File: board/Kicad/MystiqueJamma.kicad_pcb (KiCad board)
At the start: 2 copper layers, 140.4 x 114.8 mm, 143 parts, among them IC1 7805, IC10 TDA2030V, IC11 LA4425V, IC2 74HC4021D, IC3 74LS245DW, IC4 74HC4021D, IC5 CY7C1049CV33, IC6 TDA1543T, IC7 74LS245DW, IC8 TLS1233, IC9 74HC4021D, J1 Conn_01x04, K1 JAMMA-EDGE-MYSTIQUE, X2 1503_09, X4 HF15H

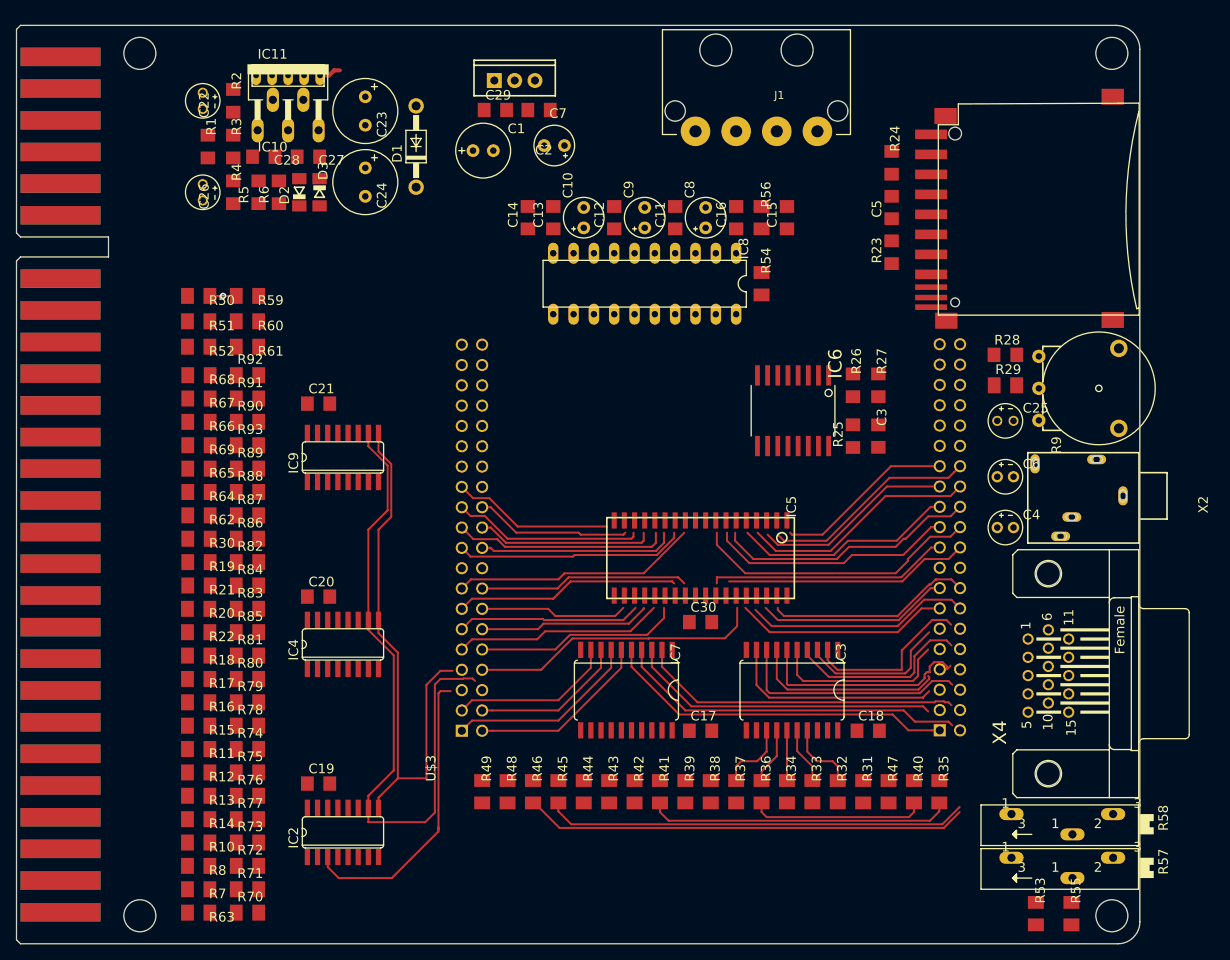
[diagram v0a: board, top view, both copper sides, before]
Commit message: Added edge cut for JTAG header
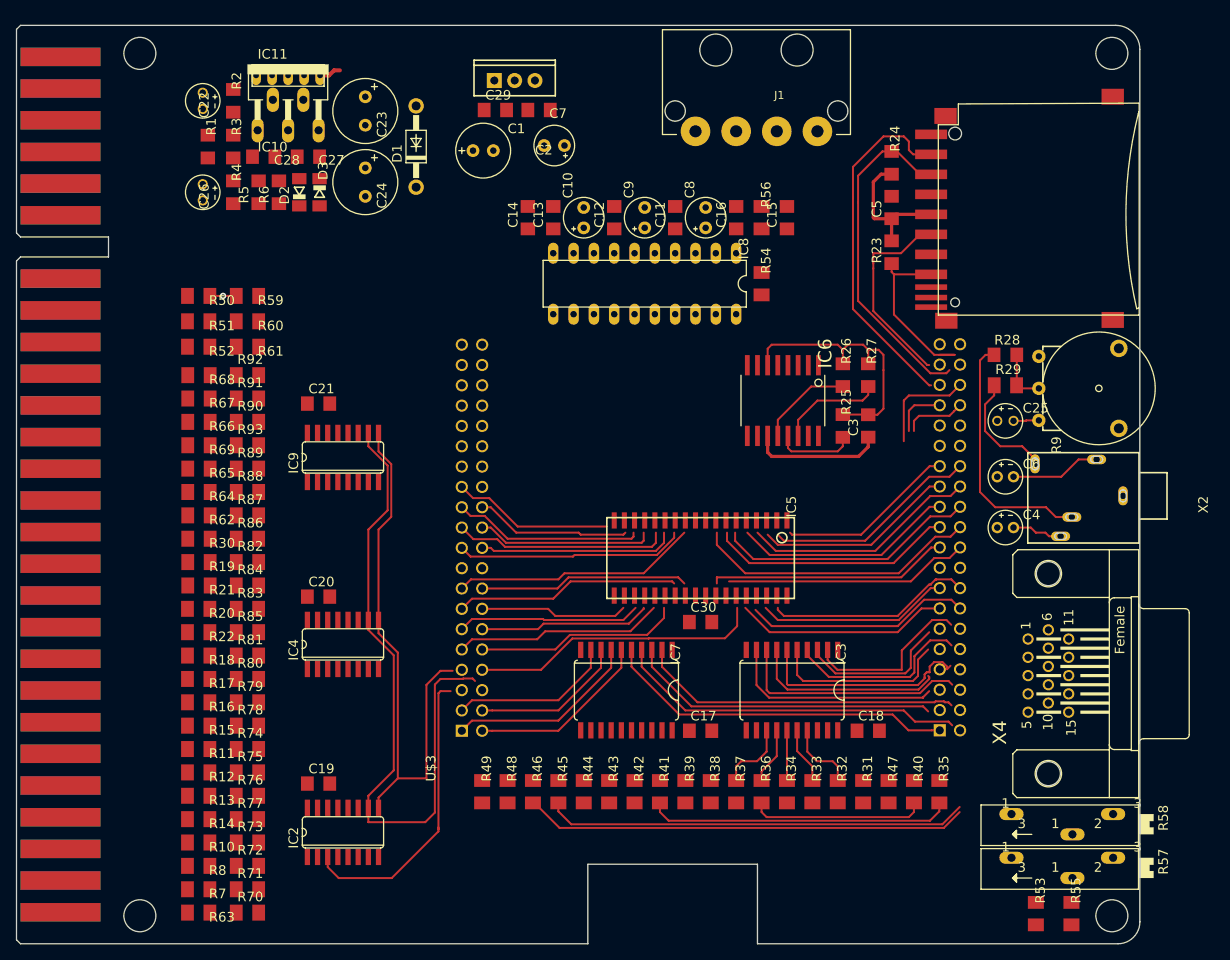
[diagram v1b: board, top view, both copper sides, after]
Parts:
- moved C3 1.80 mm to (173.4, 81.9), turned to 90 degrees
- moved R27 1.80 mm to (173.4, 75.6)
- moved IC6 1.80 mm to (162.7, 78.7)
- moved R25 1.80 mm to (170.2, 81.9), turned to 270 degrees
- moved R26 1.80 mm to (170.2, 75.6)
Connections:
- J1 pad 1: Net-(J1-Pad1) -> +12V
- J1 pad 2: Net-(J1-Pad2) -> GND
- J1 pad 3: Net-(J1-Pad3) -> GND
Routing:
- net /SD_CS: track 0.00 -> 44.4 mm
- net /SD_DATAIN: track 0.00 -> 42.6 mm
- net GND: track 0.00 -> 33.4 mm
- net Net-(R28-Pad1): track 0.00 -> 31.3 mm
- net /SD_SCLK: track 0.00 -> 25.2 mm
- net /SD_DATAOUT: track 0.00 -> 22.7 mm
- net +3V3: track 0.00 -> 17.4 mm
- net +5V: track 0.00 -> 16.6 mm
- net Net-(R29-Pad1): track 0.00 -> 14.5 mm
- net /R_A: track 0.00 -> 13.1 mm
- net Net-(U$3-PadI0_105): track 0.00 -> 12.9 mm
- net /L_A: track 0.00 -> 11.9 mm
- net /L_AUDIO: track 0.00 -> 11.3 mm
- net /DAC_VREF: track 0.00 -> 9.93 mm
- net Net-(U$3-PadI0_110): track 0.00 -> 7.85 mm
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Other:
- outline, holes or cut-outs redrawn

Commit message: Edge connector pins associated with shift registers
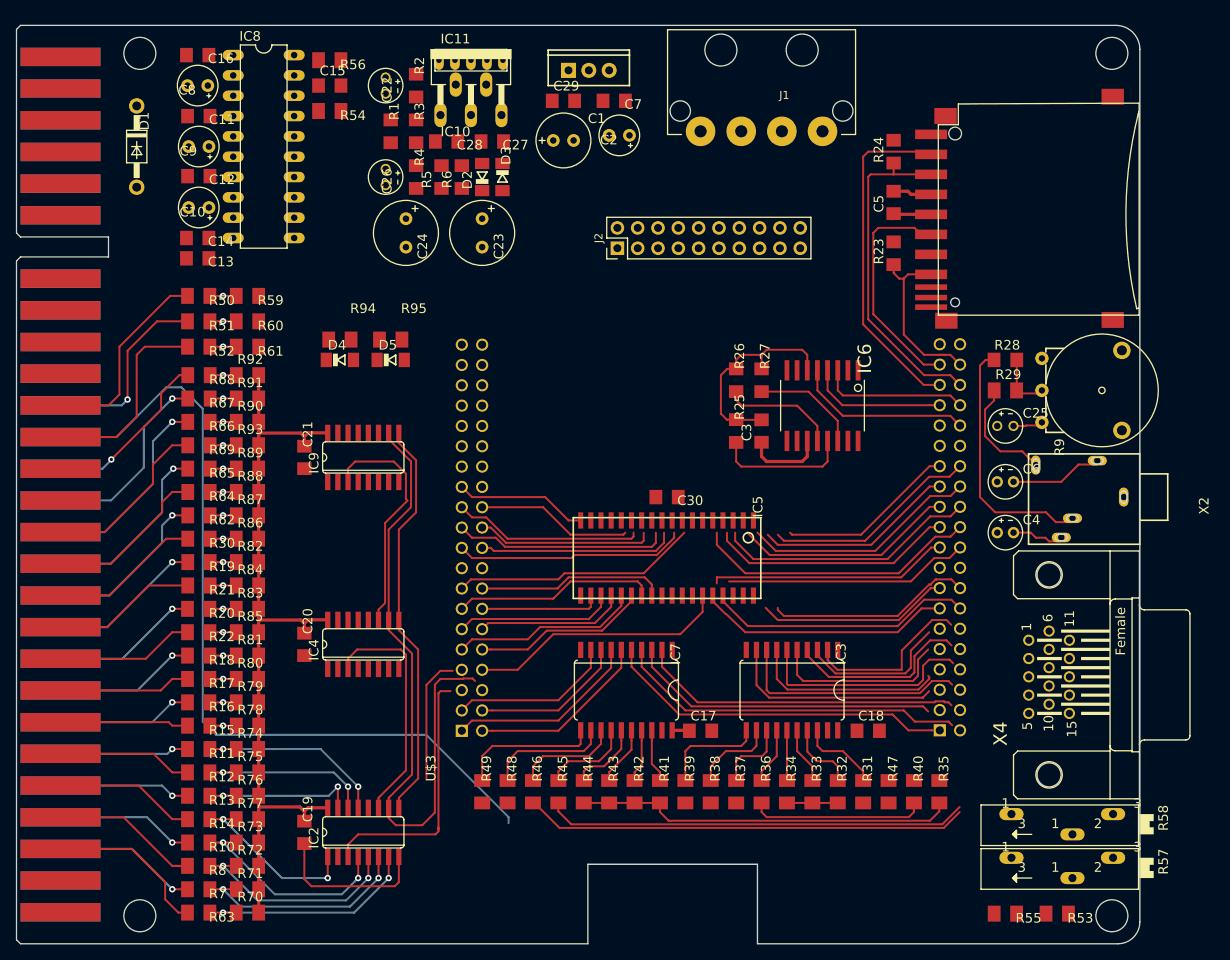
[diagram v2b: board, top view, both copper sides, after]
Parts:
- added D4: 4148, MystiqueJamma:SOD80C, F.Cu at (107.3, 73.7)
- added D5: 4148, MystiqueJamma:SOD80C, F.Cu at (113.7, 73.7)
- added J2: Conn_02x10_Odd_Even, Connector_PinHeader_2.54mm:PinHeader_2x10_P2.54mm_Vertical, F.Cu at (142.0, 59.7)
- added R94: 330, MystiqueJamma:M1206, F.Cu at (107.3, 71.1)
- added R95: 330, MystiqueJamma:M1206, F.Cu at (113.7, 71.1)
- moved C16 70.3 mm to (89.5, 35.6), turned to 180 degrees
- moved C8 65.6 mm to (89.5, 39.4), turned to 180 degrees
- moved C11 60.9 mm to (89.7, 43.2), turned to 180 degrees
- moved C15 59.5 mm to (106.0, 39.4), turned to 0 degrees
- moved R54 58.1 mm to (106.0, 42.5), turned to 180 degrees
- moved R56 57.5 mm to (106.0, 36.2), turned to 180 degrees
- moved C9 56.4 mm to (89.7, 47.0), turned to 180 degrees
- moved C12 52.2 mm to (89.7, 50.7), turned to 180 degrees
- moved IC8 50.6 mm to (97.8, 47.0), turned to 270 degrees
- moved C10 48.1 mm to (89.7, 54.6), turned to 180 degrees
- moved C13 44.7 mm to (89.5, 61.0), turned to 180 degrees
- moved C14 41.4 mm to (89.5, 58.4), turned to 180 degrees
- moved D1 34.9 mm to (81.9, 47.0), turned to 270 degrees
- moved C27 23.1 mm to (126.4, 46.4)
- moved R6 22.9 mm to (122.6, 50.8)
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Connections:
- net Net-(K1-Pad8) renamed /COIN_CT1
- net Net-(K1-PadJ) renamed /COIN_CT2
- IC9 pad 11: GND -> Net-(D4-PadA)
- K1 pad #A: Net-(K1-Pad#A) -> /P2B2
- K1 pad #B: Net-(K1-Pad#B) -> /P2B3
- K1 pad #C: Net-(K1-Pad#C) -> /P2B4
- K1 pad #D: Net-(K1-Pad#D) -> /P2B5
- K1 pad M: Net-(K1-PadM) -> GND
- K1 pad R: Net-(K1-PadR) -> /SERVICE_SW
- K1 pad S: Net-(K1-PadS) -> /TILT
- K1 pad T: Net-(K1-PadT) -> /COINSW2
- K1 pad U: Net-(K1-PadU) -> /P2START
- K1 pad V: Net-(K1-PadV) -> /P2UP
- K1 pad W: Net-(K1-PadW) -> /P2DW
- K1 pad X: Net-(K1-PadX) -> /P2LH
- K1 pad Y: Net-(K1-PadY) -> /P2RH
- K1 pad Z: Net-(K1-PadZ) -> /P2B1
- R10 pad 2: /N$62 -> /P2B4
- R11 pad 2: /N$64 -> /P2B2
- R12 pad 2: /N$63 -> /P1B2
- R13 pad 2: /N$65 -> /P2B3
- R14 pad 2: /N$66 -> /P1B3
- R15 pad 2: /N$68 -> /P1B1
- R16 pad 2: /N$67 -> /P2B1
- R17 pad 2: /N$69 -> /P1RH
- R18 pad 2: /N$70 -> /P2RH
- R19 pad 2: /N$72 -> /P2DW
- R20 pad 2: /N$73 -> /P2LH
- R21 pad 2: /N$74 -> /P1DW
- R22 pad 2: /N$76 -> /P1LH
- R30 pad 2: /N$75 -> /P1UP
- R62 pad 2: /N$77 -> /P2UP
- R63 pad 2: /N$47 -> /P1B5
- R64 pad 2: /N$78 -> /P1START
- R65 pad 2: /N$80 -> /P2START
- R66 pad 2: /N$79 -> /COINSW2
- R67 pad 2: /N$81 -> /TILT
- R68 pad 2: /N$82 -> /SERVICE_SW
- R69 pad 2: /VGA_DETECT -> /COINSW1
- R7 pad 2: /N$46 -> /P2B5
- R8 pad 2: /N$61 -> /P1B4
- U$3 pad I0_1: Net-(U$3-PadI0_1) -> /G2
- U$3 pad I0_10: Net-(U$3-PadI0_10) -> /B2
- U$3 pad I0_101: Net-(U$3-PadI0_101) -> /SD_SCLK
- U$3 pad I0_103: Net-(U$3-PadI0_103) -> /SD_DATAOUT
- U$3 pad I0_104: Net-(U$3-PadI0_104) -> /SD_CS
- U$3 pad I0_105: Net-(U$3-PadI0_105) -> /SD_DATAIN
- U$3 pad I0_106: Net-(U$3-PadI0_106) -> /IS2_WS
- U$3 pad I0_110: Net-(U$3-PadI0_110) -> /I2S_BCK
- U$3 pad I0_112: Net-(U$3-PadI0_112) -> /I2S_DATA
- U$3 pad I0_115: Net-(U$3-PadI0_115) -> /SRAM_A0
- U$3 pad I0_119: Net-(U$3-PadI0_119) -> /SRAM_A1
- U$3 pad I0_120: Net-(U$3-PadI0_120) -> /SRAM_A2
- U$3 pad I0_121: Net-(U$3-PadI0_121) -> /SRAM_A3
- U$3 pad I0_124: Net-(U$3-PadI0_124) -> /SRAM_A4
- U$3 pad I0_125: Net-(U$3-PadI0_125) -> /SRAM_CE
- U$3 pad I0_126: Net-(U$3-PadI0_126) -> /SRAM_IO0
- U$3 pad I0_127: Net-(U$3-PadI0_127) -> /SRAM_IO1
- U$3 pad I0_128: Net-(U$3-PadI0_128) -> /SRAM_IO6
- U$3 pad I0_129: Net-(U$3-PadI0_129) -> /SRAM_IO7
- U$3 pad I0_132: Net-(U$3-PadI0_132) -> /SRAM_A18
- U$3 pad I0_133: Net-(U$3-PadI0_133) -> /SRAM_A17
- U$3 pad I0_135: Net-(U$3-PadI0_135) -> /SRAM_A16
- U$3 pad I0_136: Net-(U$3-PadI0_136) -> /SRAM_A15
- U$3 pad I0_137: Net-(U$3-PadI0_137) -> /R0
- U$3 pad I0_138: Net-(U$3-PadI0_138) -> /R1
- U$3 pad I0_141: Net-(U$3-PadI0_141) -> /R2
- U$3 pad I0_142: Net-(U$3-PadI0_142) -> /R3
- U$3 pad I0_143: Net-(U$3-PadI0_143) -> /G0
- U$3 pad I0_144: Net-(U$3-PadI0_144) -> /G1
- U$3 pad I0_2: Net-(U$3-PadI0_2) -> /G3
- U$3 pad I0_3: Net-(U$3-PadI0_3) -> /B0
- U$3 pad I0_33: Net-(U$3-PadI0_33) -> /CNTR_DAT
- U$3 pad I0_34: Net-(U$3-PadI0_34) -> /CNTR_CLK
- U$3 pad I0_38: Net-(U$3-PadI0_38) -> /CNTR_LATCH
- U$3 pad I0_39: Net-(U$3-PadI0_39) -> /SRAM_OE
- U$3 pad I0_42: Net-(U$3-PadI0_42) -> /SRAM_A13
- U$3 pad I0_43: Net-(U$3-PadI0_43) -> /SRAM_A14
- U$3 pad I0_44: Net-(U$3-PadI0_44) -> /SRAM_A11
- U$3 pad I0_46: Net-(U$3-PadI0_46) -> /SRAM_A12
- U$3 pad I0_49: Net-(U$3-PadI0_49) -> /SRAM_IO4
- U$3 pad I0_50: Net-(U$3-PadI0_50) -> /SRAM_A10
- U$3 pad I0_51: Net-(U$3-PadI0_51) -> /SRAM_IO2
- U$3 pad I0_52: Net-(U$3-PadI0_52) -> /SRAM_IO5
- U$3 pad I0_53: Net-(U$3-PadI0_53) -> /SRAM_IO3
- U$3 pad I0_54: Net-(U$3-PadI0_54) -> /SRAM_WE
- U$3 pad I0_55: Net-(U$3-PadI0_55) -> /SRAM_A5
- U$3 pad I0_58: Net-(U$3-PadI0_58) -> /SRAM_A6
- U$3 pad I0_59: Net-(U$3-PadI0_59) -> /SRAM_A7
- U$3 pad I0_60: Net-(U$3-PadI0_60) -> /SRAM_A8
- U$3 pad I0_64: Net-(U$3-PadI0_64) -> /SRAM_A9
- U$3 pad I0_7: Net-(U$3-PadI0_7) -> /B1
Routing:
- net /JAMMA-CSYNC: track 0.00 -> 104.5 mm
- net +3V3: track 17.4 -> 103.1 mm
- net Net-(U$3-PadI0_39): track 36.4 -> 0.00 mm
- net Net-(U$3-PadI0_127): track 35.8 -> 0.00 mm
- net /SRAM_IO1: track 0.00 -> 35.8 mm
- net /SRAM_A16: track 0.00 -> 33.4 mm
- net Net-(U$3-PadI0_125): track 32.8 -> 0.00 mm
- net /SRAM_CE: track 0.00 -> 32.8 mm
- net /SRAM_OE: track 0.00 -> 32.6 mm
- net /SRAM_A15: track 0.00 -> 31.8 mm
- net Net-(U$3-PadI0_51): track 30.7 -> 0.00 mm
- net /SRAM_IO2: track 0.00 -> 30.7 mm
- net Net-(U$3-PadI0_129): track 30.6 -> 0.00 mm
- net /SRAM_IO7: track 0.00 -> 30.6 mm
- net Net-(U$3-PadI0_126): track 30.6 -> 0.00 mm
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
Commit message: First completed layout
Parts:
- moved D1 49.2 mm to (131.1, 43.9), turned to 90 degrees
- moved R54 5.71 mm to (106.0, 48.3)
- moved R6 3.94 mm to (118.6, 50.8)
- moved C15 3.81 mm to (106.0, 43.2)
- moved D4 3.43 mm to (107.3, 77.1)
- moved D5 3.43 mm to (113.7, 77.1)
- moved R94 3.43 mm to (107.3, 74.5)
- moved R95 3.43 mm to (113.7, 74.5)
- moved C13 2.54 mm to (89.5, 58.4)
- moved C14 2.54 mm to (89.5, 61.0)
- moved R56 2.03 mm to (106.0, 38.2)
- moved C2 1.65 mm to (143.8, 46.2)
- moved C1 1.52 mm to (136.8, 46.2)
- moved C29 1.52 mm to (136.8, 41.3)
- moved C7 1.52 mm to (143.1, 41.3)
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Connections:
- C25 pad +: Net-(C25-Pad+) -> /AUD-IN
- IC10 pad 1: Net-(C25-Pad+) -> /AUD-IN
- IC11 pad 1: Net-(C25-Pad+) -> /AUD-IN
- J2 pad 1: Net-(J2-Pad1) -> /IO_100
- J2 pad 10: Net-(J2-Pad10) -> /IO_71
- J2 pad 11: Net-(J2-Pad11) -> /IO_68
- J2 pad 12: Net-(J2-Pad12) -> /IO_69
- J2 pad 13: Net-(J2-Pad13) -> /IO_66
- J2 pad 14: Net-(J2-Pad14) -> /IO_67
- J2 pad 15: Net-(J2-Pad15) -> /IO_113
- J2 pad 16: Net-(J2-Pad16) -> /IO_65
- J2 pad 17: Net-(J2-Pad17) -> /IO_111
- J2 pad 18: Net-(J2-Pad18) -> /IO_114
- J2 pad 2: Net-(J2-Pad2) -> +3V3
- J2 pad 20: Net-(J2-Pad20) -> /AUD-IN
- J2 pad 3: Net-(J2-Pad3) -> /IO_91
- J2 pad 4: Net-(J2-Pad4) -> /IO_99
- J2 pad 5: Net-(J2-Pad5) -> /IO_89
- J2 pad 6: Net-(J2-Pad6) -> /IO_90
- J2 pad 7: Net-(J2-Pad7) -> /IO_72
- J2 pad 8: Net-(J2-Pad8) -> /IO_88
- J2 pad 9: Net-(J2-Pad9) -> /IO_70
- K1 pad 3: +5V -> NC3
- K1 pad 4: +5V -> NC4
- K1 pad 5: -5V -> NC5
- K1 pad C: +5V -> NCC
- K1 pad D: +5V -> NCD
- K1 pad E: -5V -> NCE
- R3 pad 2: Net-(C25-Pad+) -> /AUD-IN
- U$3 pad I0_100: Net-(U$3-PadI0_100) -> /IO_100
- U$3 pad I0_111: Net-(U$3-PadI0_111) -> /IO_111
- U$3 pad I0_113: Net-(U$3-PadI0_113) -> /IO_113
- U$3 pad I0_114: Net-(U$3-PadI0_114) -> /IO_114
- U$3 pad I0_65: Net-(U$3-PadI0_65) -> /IO_65
- U$3 pad I0_66: Net-(U$3-PadI0_66) -> /IO_66
- U$3 pad I0_67: Net-(U$3-PadI0_67) -> /IO_67
- U$3 pad I0_68: Net-(U$3-PadI0_68) -> /IO_68
- U$3 pad I0_69: Net-(U$3-PadI0_69) -> /IO_69
- U$3 pad I0_70: Net-(U$3-PadI0_70) -> /IO_70
- U$3 pad I0_71: Net-(U$3-PadI0_71) -> /IO_71
- U$3 pad I0_72: Net-(U$3-PadI0_72) -> /IO_72
- U$3 pad I0_88: Net-(U$3-PadI0_88) -> /IO_88
- U$3 pad I0_89: Net-(U$3-PadI0_89) -> /IO_89
- U$3 pad I0_90: Net-(U$3-PadI0_90) -> /IO_90
- U$3 pad I0_91: Net-(U$3-PadI0_91) -> /IO_91
- U$3 pad I0_99: Net-(U$3-PadI0_99) -> /IO_99
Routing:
- net +12V: track 0.00 -> 372.8 mm, vias 0 -> 5
- net GND: track 51.8 -> 306.1 mm, vias 0 -> 61
- net Net-(C16-Pad1): track 0.00 -> 222.0 mm
- net +3V3: track 103.1 -> 314.3 mm, vias 0 -> 7
- net /VGA-RED: track 6.35 -> 213.4 mm, vias 0 -> 2
- net /VGA-GREEN: track 21.9 -> 225.5 mm, vias 0 -> 2
- net +5V: track 12.1 -> 201.7 mm, vias 0 -> 6
- net /VGA-BLUE: track 47.6 -> 233.3 mm, vias 0 -> 2
- net Net-(C14-Pad1): track 0.00 -> 184.7 mm
- net /AUD-IN: track 0.00 -> 148.3 mm
- net /VGA_DETECT: track 0.00 -> 141.8 mm, vias 0 -> 1
- net /BURST_GATE: track 0.00 -> 86.3 mm, vias 0 -> 1
- net /IO_114: track 0.00 -> 68.8 mm, vias 0 -> 1
- net /IO_113: track 0.00 -> 64.0 mm, vias 0 -> 1
- net /IO_111: track 0.00 -> 61.4 mm, vias 0 -> 1
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- added copper zone on B.Cu, net GND
- added copper zone on F.Cu, net GND

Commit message: routing and footprints enhancement
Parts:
- removed U$3: C4E6-K, MystiqueJamma:E6V33_BELOW
- removed X2: 1503_09, MystiqueJamma:1503_09
- added EVB1: C4E6-K, MystiqueJamma:E6V33_BELOW, F.Cu at (153.7, 146.7)
- added J3: FPGA PWR, Connector_PinHeader_2.54mm:PinHeader_1x02_P2.54mm_Horizontal, F.Cu at (165.5, 136.0)
- added J5: 1503_09, MystiqueJamma:1503_09, F.Cu at (207.4, 90.8)
- moved C13 2.67 mm to (89.5, 61.1)
- moved C14 2.54 mm to (89.5, 58.4)
- turned R3 to 90 degrees
- renumbered U$2 to J4, X4 to J6
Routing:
- net +5V: track 201.7 -> 250.9 mm, vias 6 -> 7
- net Net-(C13-Pad1): track 4.19 -> 12.5 mm
- net GND: track 306.1 -> 298.8 mm, vias 61 -> 64
- net +12V: track 372.8 -> 367.1 mm
- net Net-(C22-Pad+): track 10.9 -> 15.0 mm
- net Net-(C14-Pad1): track 184.7 -> 181.5 mm
- net /JAMMA-CSYNC: track 138.5 -> 135.4 mm
- net /VGA-GREEN: track 225.5 -> 222.8 mm
- net /VGA-RED: track 213.4 -> 210.7 mm
- net /JAMMA-BLUE: track 25.1 -> 22.6 mm
- net /JAMMA-GREEN: track 23.8 -> 21.6 mm
- net /VGA_DETECT: track 141.8 -> 140.0 mm
- net /VGA-BLUE: track 233.3 -> 232.0 mm
- net /BURST_GATE: track 86.3 -> 87.6 mm
- net Net-(R29-Pad1): track 14.5 -> 15.6 mm
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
